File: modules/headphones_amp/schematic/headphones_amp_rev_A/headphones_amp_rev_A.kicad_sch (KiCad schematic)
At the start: 24 parts, among them Q1 BC140, Q2 BC160, Q3 BC548, Q4 BC557, Q5 BC548, Q6 BC548

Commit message: added new references to the PPL
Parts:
- removed D1, D2, D3: 1N4148, Diode_THT:D_DO-35_SOD27_P7.62mm_Horizontal, symbol Diode:1N4148
- added C3: 220µ, Capacitor_THT:CP_Radial_D10.0mm_P5.00mm, symbol Device:C_Polarized
- added Q7: BC548, Package_TO_SOT_THT:TO-92L_Inline_Wide, symbol Transistor_BJT:BC548
- added R13: 3.3k, Resistor_THT:R_Axial_DIN0207_L6.3mm_D2.5mm_P10.16mm_Horizontal, symbol Device:R_US
- added R14: 1.5k, Resistor_THT:R_Axial_DIN0207_L6.3mm_D2.5mm_P10.16mm_Horizontal, symbol Device:R_US
- added R15: 820, Resistor_THT:R_Axial_DIN0207_L6.3mm_D2.5mm_P10.16mm_Horizontal, symbol Device:R_US
- added R16: 15k, Resistor_THT:R_Axial_DIN0207_L6.3mm_D2.5mm_P10.16mm_Horizontal, symbol Device:R_US
- added R17: 56k, Resistor_THT:R_Axial_DIN0207_L6.3mm_D2.5mm_P10.16mm_Horizontal, symbol Device:R_US
- added R18: 33k, Resistor_THT:R_Axial_DIN0207_L6.3mm_D2.5mm_P10.16mm_Horizontal, symbol Device:R_US
- added R19: 10k, Resistor_THT:R_Axial_DIN0207_L6.3mm_D2.5mm_P10.16mm_Horizontal, symbol Device:R_US
- added RV1: 820, Potentiometer_THT:Potentiometer_Bourns_3296W_Vertical, symbol Device:R_Potentiometer_US
- added RV2: 2.2k, Potentiometer_THT:Potentiometer_Bourns_3296W_Vertical, symbol Device:R_Potentiometer_US
- added TP1, TP2: TestPoint, TestPoint:TestPoint_Pad_D2.0mm, symbol Connector:TestPoint
- C1: value 100µ -> 220µ
- R5: value 1.2k -> 2.2k
- R8: value 330 -> 470
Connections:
- net +12V: now also R19.2
- net GND: now also R13.2, R16.2, R18.2
- net at Q1.2 (B), R5.2: now also Q7.1 (C), R14.1, TP1.1
- net at C1.2: now also R13.1
- net at Q2.2 (B), Q5.1 (C): now also Q7.3 (E), R15.2, TP2.1
- net at Q5.2 (B): now also C3.2, RV2.2
- new net: R17.1, R19.1
- new net: R17.2, RV2.1
- new net: R16.1, R18.1, RV2.3
- new net: R15.1, RV1.3
- new net: R14.2, RV1.1
- new net: Q7.2 (B), RV1.2
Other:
- moved on the sheet: C1, C2, D4, Q1, Q2, Q3, Q4, Q5, Q6, R1, R10, R11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

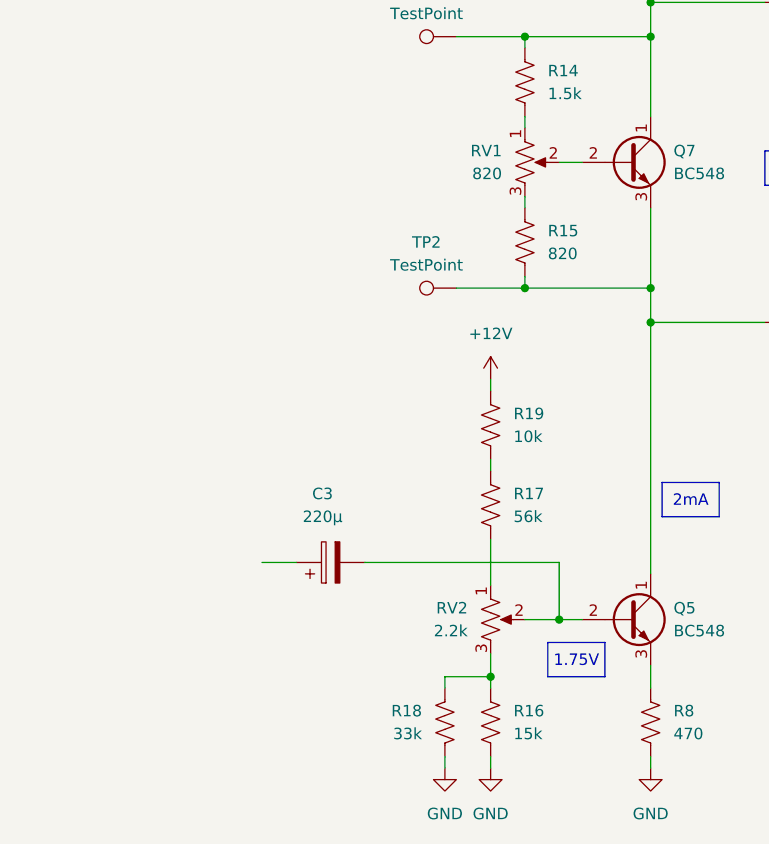
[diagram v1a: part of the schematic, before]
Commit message: updated the calculations/simulations/schematic for the headphones amp
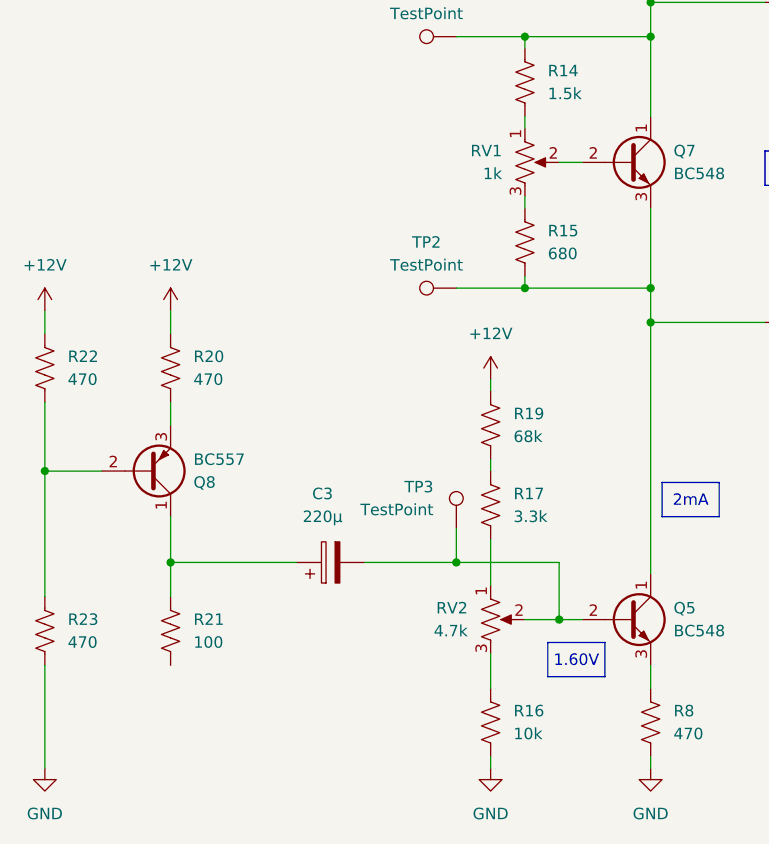
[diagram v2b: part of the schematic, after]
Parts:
- removed R18: 33k, Resistor_THT:R_Axial_DIN0207_L6.3mm_D2.5mm_P10.16mm_Horizontal, symbol Device:R_US
- added Q8: BC557, Package_TO_SOT_THT:TO-92L_Inline_Wide, symbol Transistor_BJT:BC557
- added R20, R22, R23: 470, Resistor_THT:R_Axial_DIN0207_L6.3mm_D2.5mm_P10.16mm_Horizontal, symbol Device:R_US
- added R21: 100, Resistor_THT:R_Axial_DIN0207_L6.3mm_D2.5mm_P10.16mm_Horizontal, symbol Device:R_US
- added TP3: TestPoint, TestPoint:TestPoint_Pad_D2.0mm, symbol Connector:TestPoint
- R15: value 820 -> 680
- R16: value 15k -> 10k
- R17: value 56k -> 3.3k
- R19: value 10k -> 68k
- RV1: value 820 -> 1k
- RV2: value 2.2k -> 4.7k
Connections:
- net +12V: now also R20.1, R22.1
- net GND: now also R23.2
- net at C3.2, Q5.2 (B), RV2.2: now also TP3.1
- net at C3.1: now also Q8.1 (C), R21.1
- new net: Q8.2 (B), R22.2, R23.1
- new net: Q8.3 (E), R20.2

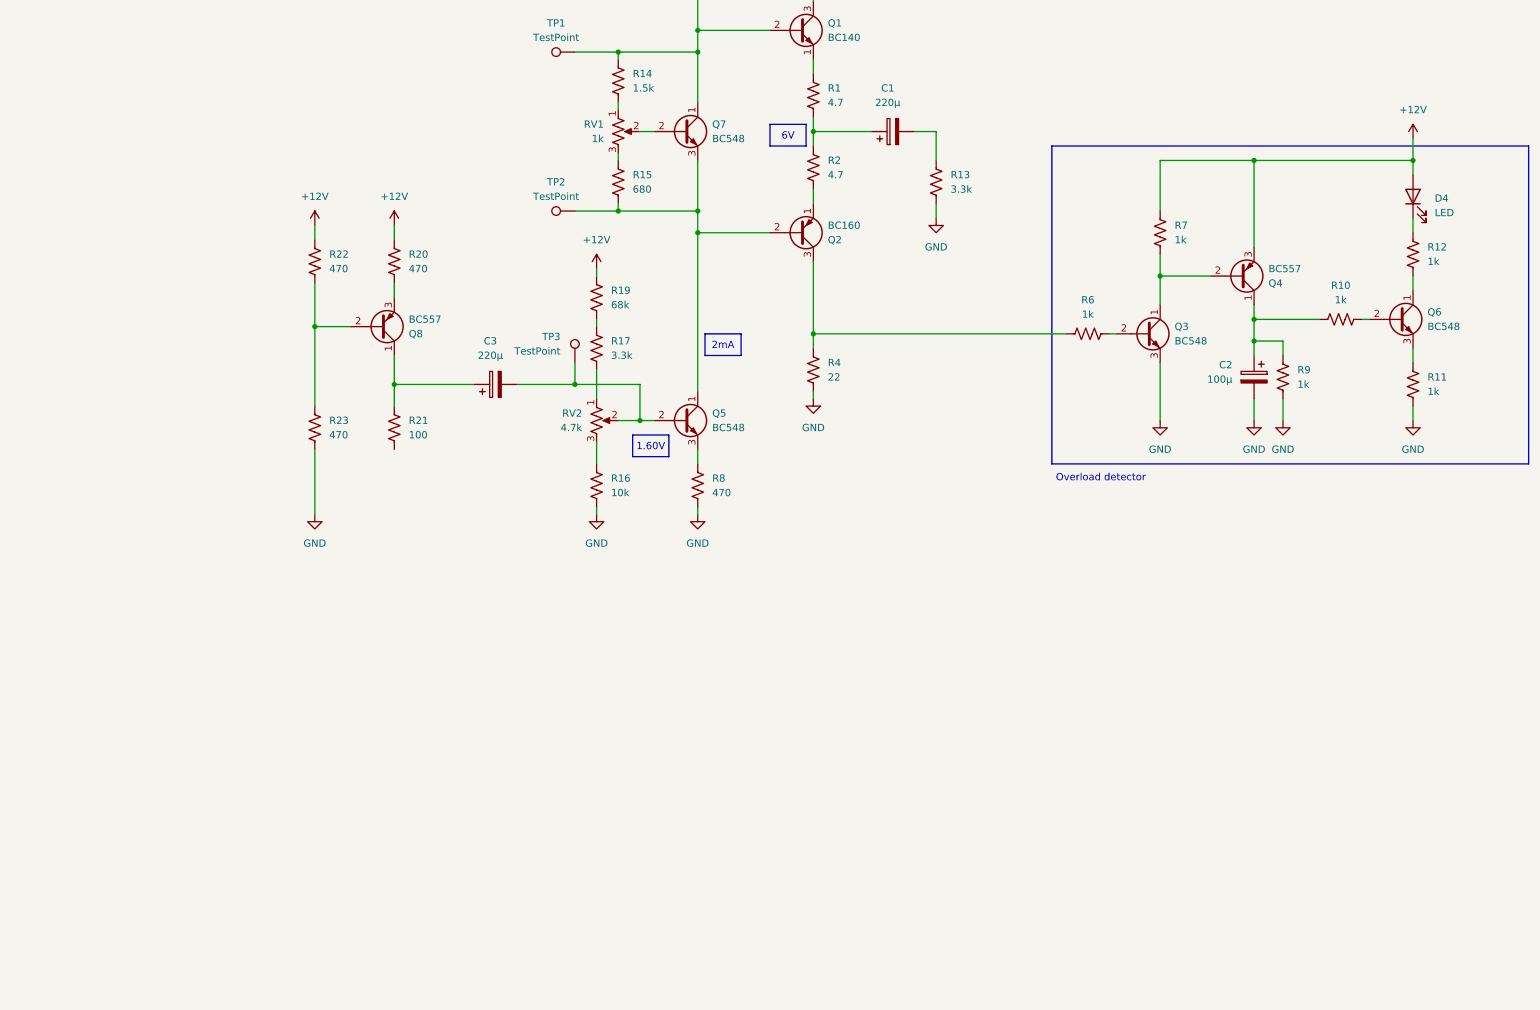
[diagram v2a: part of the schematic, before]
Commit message: added proper silkscreen on PTV potentiometer
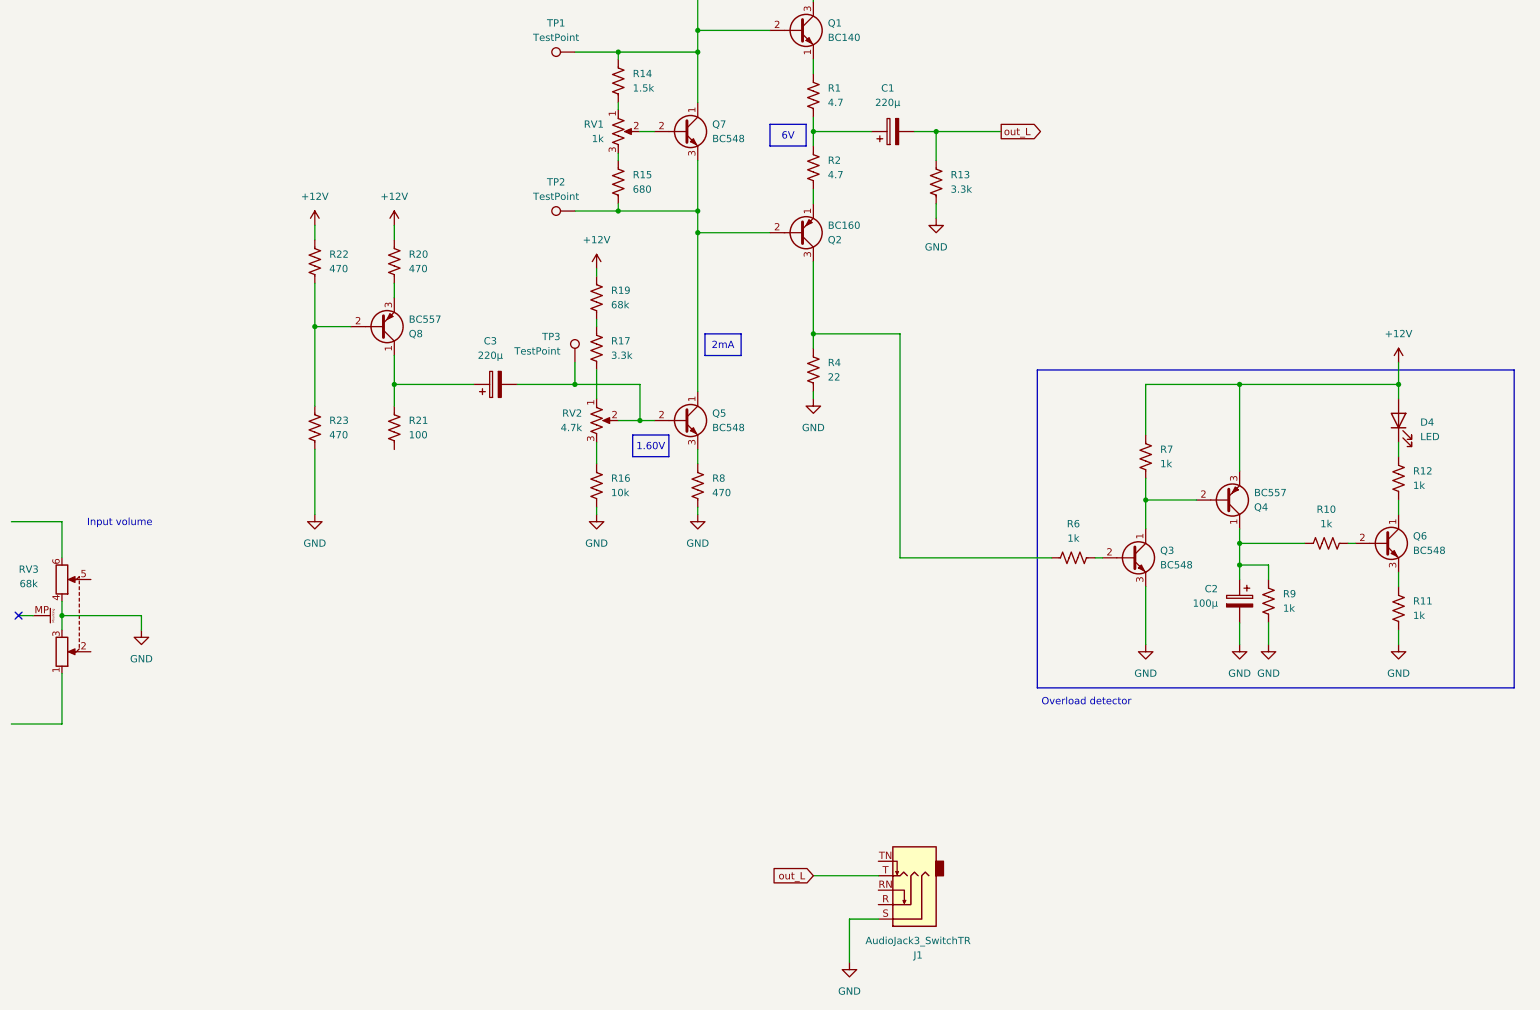
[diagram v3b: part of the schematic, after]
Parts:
- added J1: AudioJack3_SwitchTR, Connector_Audio:Jack_6.35mm_Neutrik_NRJ6HM-1-PRE_Horizontal, symbol Connector_Audio:AudioJack3_SwitchTR
- added RV3: 68k, Potentiometer_THT:Potentiometer_Bourns_PTV112-4_Dual_Vertical, symbol Device:R_Potentiometer_Dual_MountingPin
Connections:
- net GND: now also J1.S, RV3.3, RV3.4
- net out_L: now reaches C1.2, R13.1
- net out_L: now also J1.T
- no-connect marks 0 -> 1
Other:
- note added: "Input volume"
- moved on the sheet: C2, D4, Q3, Q4, Q6, R10, R11, R12, R6, R7, R9
